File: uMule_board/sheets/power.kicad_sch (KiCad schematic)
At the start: 38 parts, among them Q8 AON6407, U18 TPS62933DRLR, U22 INA219AxD, U28 TLV761

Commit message: all main componenst added. Prepared to change MCU. SCH almost ready
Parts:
- removed D14: SS34, Diode_SMD:D_SMA, symbol PCM_Diode_Schottky_AKL:SS34
- renumbered C42 to C1, C41 to C10, C43 to C11, C45 to C12, C11 to C13, C12 to C14, C13 to C15, C14 to C16, C38 to C2, C39 to C3, C40 to C4, C44 to C5, C46 to C6, C47 to C7, C35 to C8, C37 to C9, D16 to D2, D20 to D3, D17 to D4, D18 to D5, D19 to D6, F4 to F1, F5 to F2, Q8 to Q1, R59 to R1, R62 to R2, R72 to R3, R58 to R4, R63 to R5, R73 to R6, R60 to R7, R61 to R8, R68 to R9, U18 to U1, U28 to U2, U22 to U3

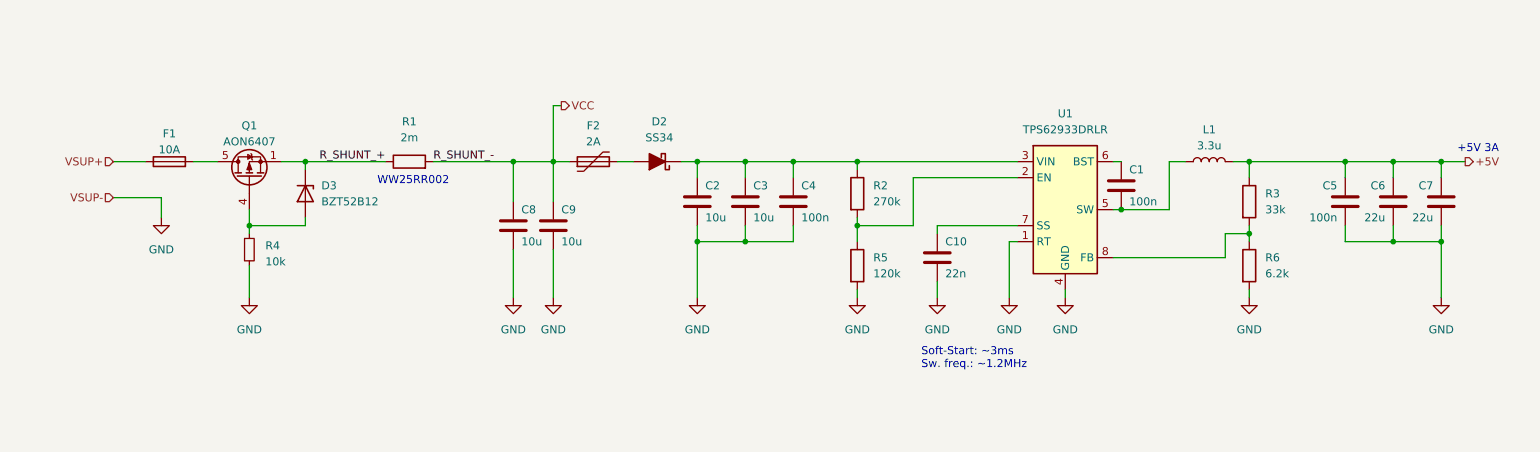
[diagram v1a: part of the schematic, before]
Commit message: Finished schematics. Now ready for PCB
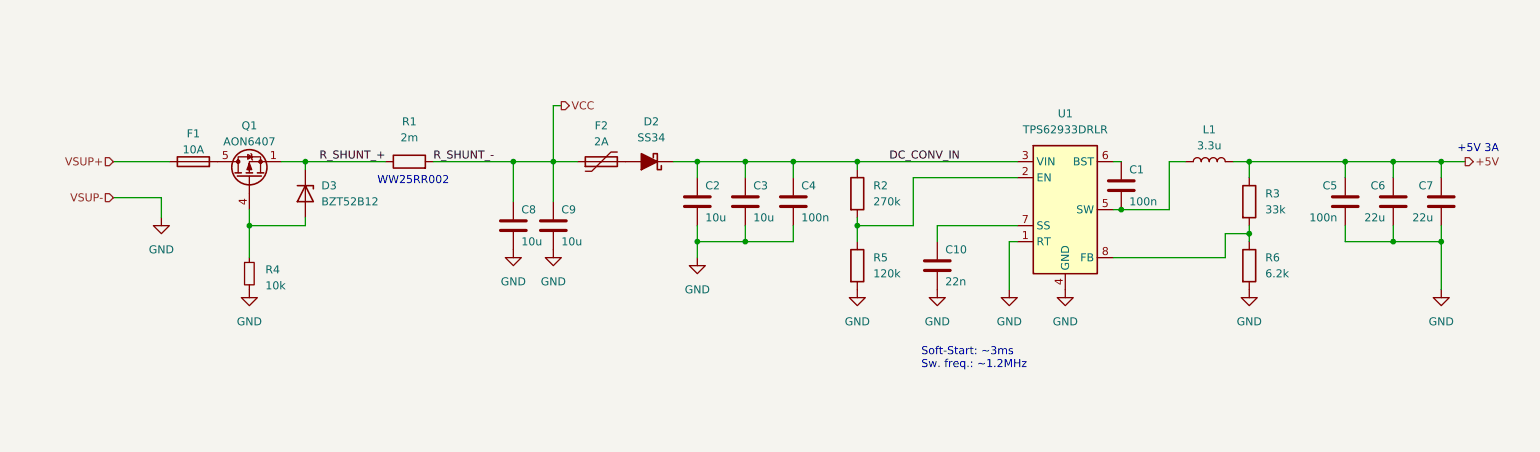
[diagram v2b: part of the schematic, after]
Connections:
- net DC_CONV_IN: now reaches C2.1, C3.1, C4.1, D2.1 (K), R2.1, U1.3 (VIN)
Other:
- moved on the sheet: C10, D2, F1, F2, R4

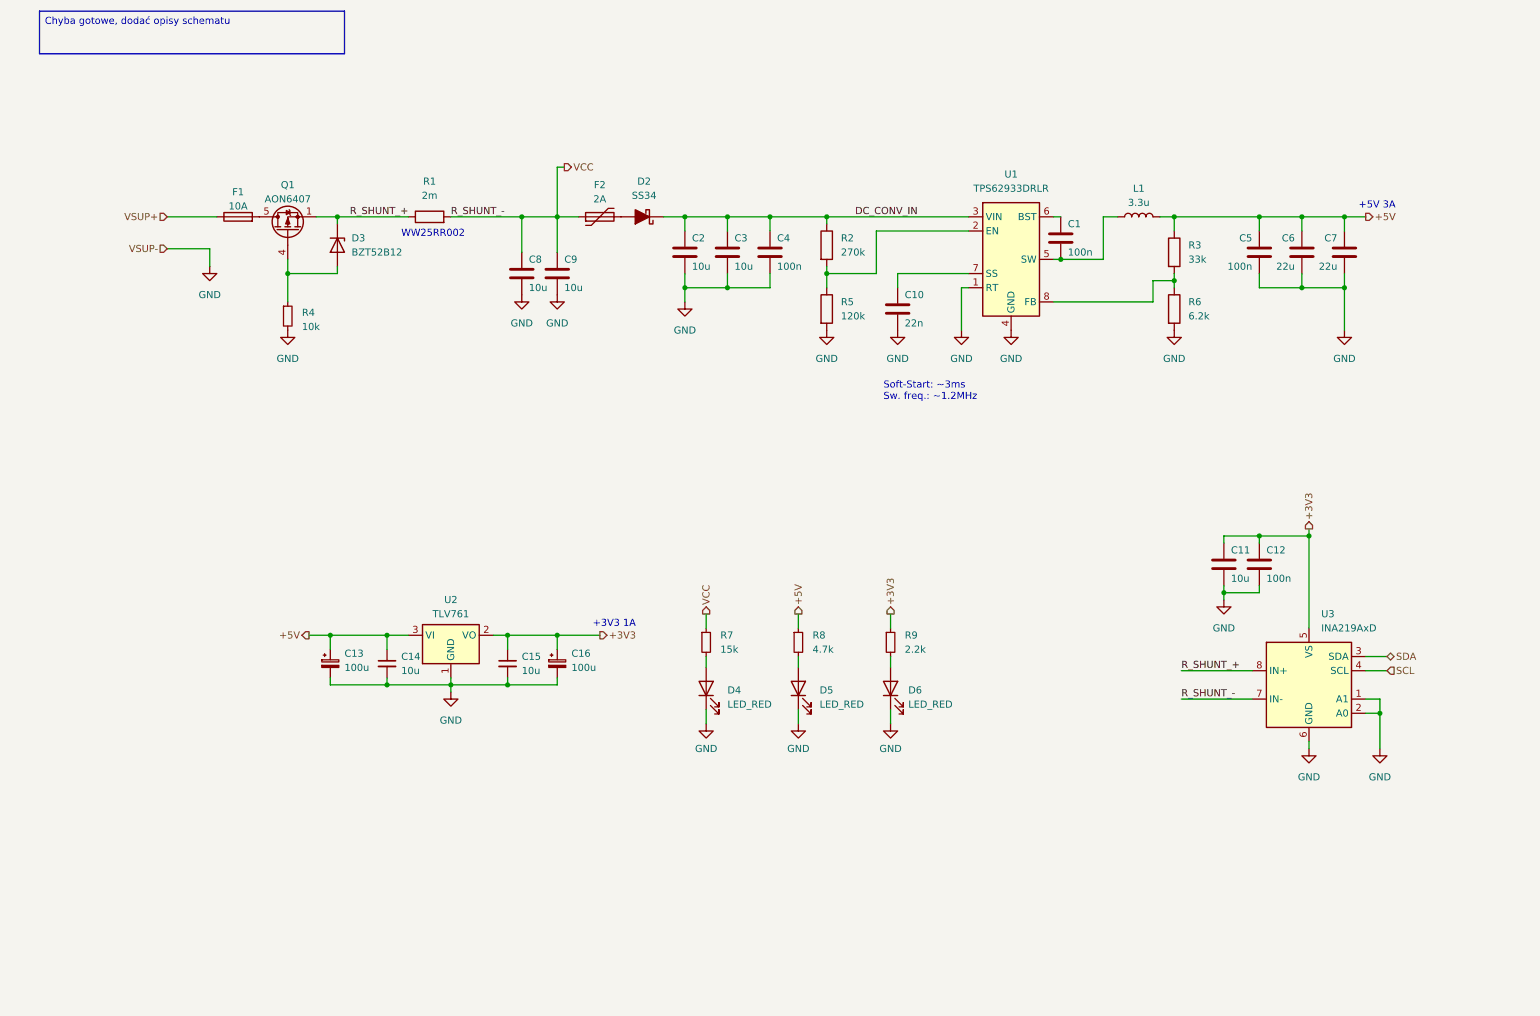
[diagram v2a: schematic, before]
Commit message: Started working on PCB. Ditched high power outputs. Focusing on photodiodes. One commit closer to order
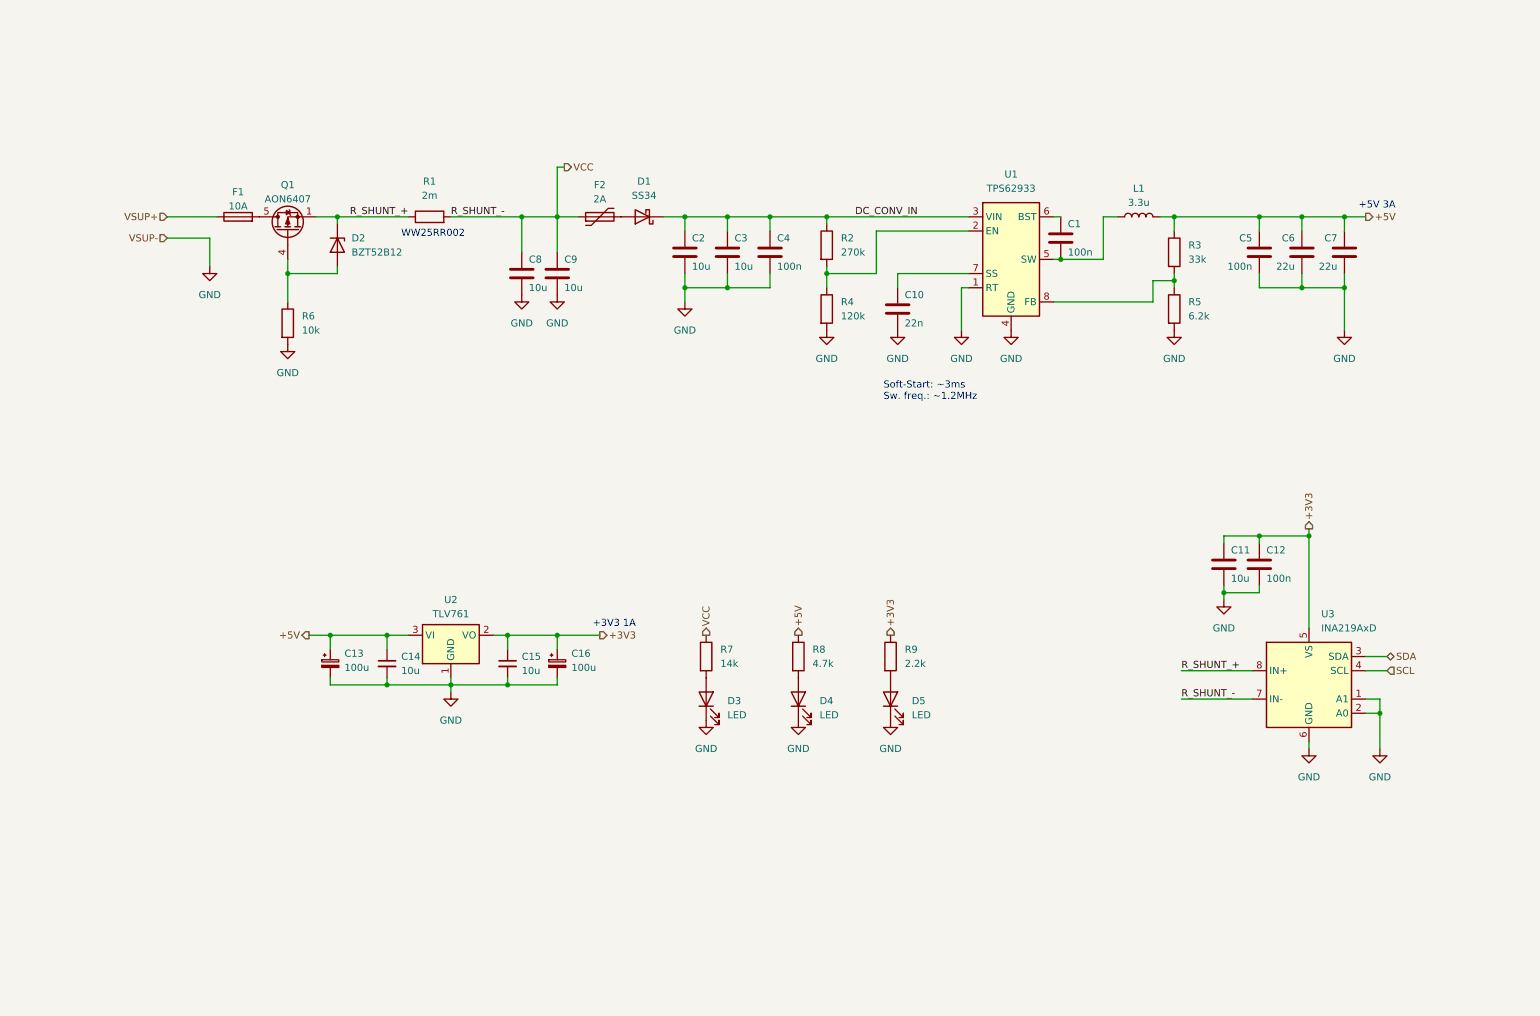
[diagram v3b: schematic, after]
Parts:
- removed D2: SS34, Diode_SMD:D_SMA, symbol PCM_Diode_Schottky_AKL:SS34
- removed D6: LED_RED, LED_SMD:LED_0603_1608Metric, symbol Device:LED
- removed R4: 10k, Resistor_SMD:R_0603_1608Metric, symbol Device:R_Small
- removed R7: 15k, Resistor_SMD:R_0603_1608Metric, symbol Device:R_Small
- removed R8: 4.7k, Resistor_SMD:R_0603_1608Metric, symbol Device:R_Small
- removed R9: 2.2k, Resistor_SMD:R_0603_1608Metric, symbol Device:R_Small
- added D1: SS34, Diode_SMD:D_SMA, symbol Diode:SS34
- added D3: LED, LED_SMD:LED_0603_1608Metric_Pad1.05x0.95mm_HandSolder, symbol Device:LED
- added R6: 10k, Resistor_SMD:R_0603_1608Metric, symbol Device:R
- added R7: 14k, Resistor_SMD:R_0603_1608Metric, symbol Device:R
- added R8: 4.7k, Resistor_SMD:R_0603_1608Metric, symbol Device:R
- added R9: 2.2k, Resistor_SMD:R_0603_1608Metric, symbol Device:R
- D4, D5: value LED_RED -> LED; footprint LED_SMD:LED_0603_1608Metric -> LED_SMD:LED_0603_1608Metric_Pad1.05x0.95mm_HandSolder
- U1: value TPS62933DRLR -> TPS62933
- renumbered D3 to D2, R5 to R4, R6 to R5
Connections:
- net +3V3: now also R9.1
- net +5V: now also R8.1
- net DC_CONV_IN: now also D1.1 (K)
- net GND: now also D3.1 (K), R6.2
- net VCC: now also R7.1
- net at D4.2 (A): now also R8.2
- net at F2.2: now also D1.2 (A)
- net at D5.2 (A): now also R9.2
- net at D2.2 (A), Q1.4 (G): now also R6.1
- new net: D3.2 (A), R7.2
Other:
- title: (none) -> uMule_board

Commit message: removed half phototransistors, etc.
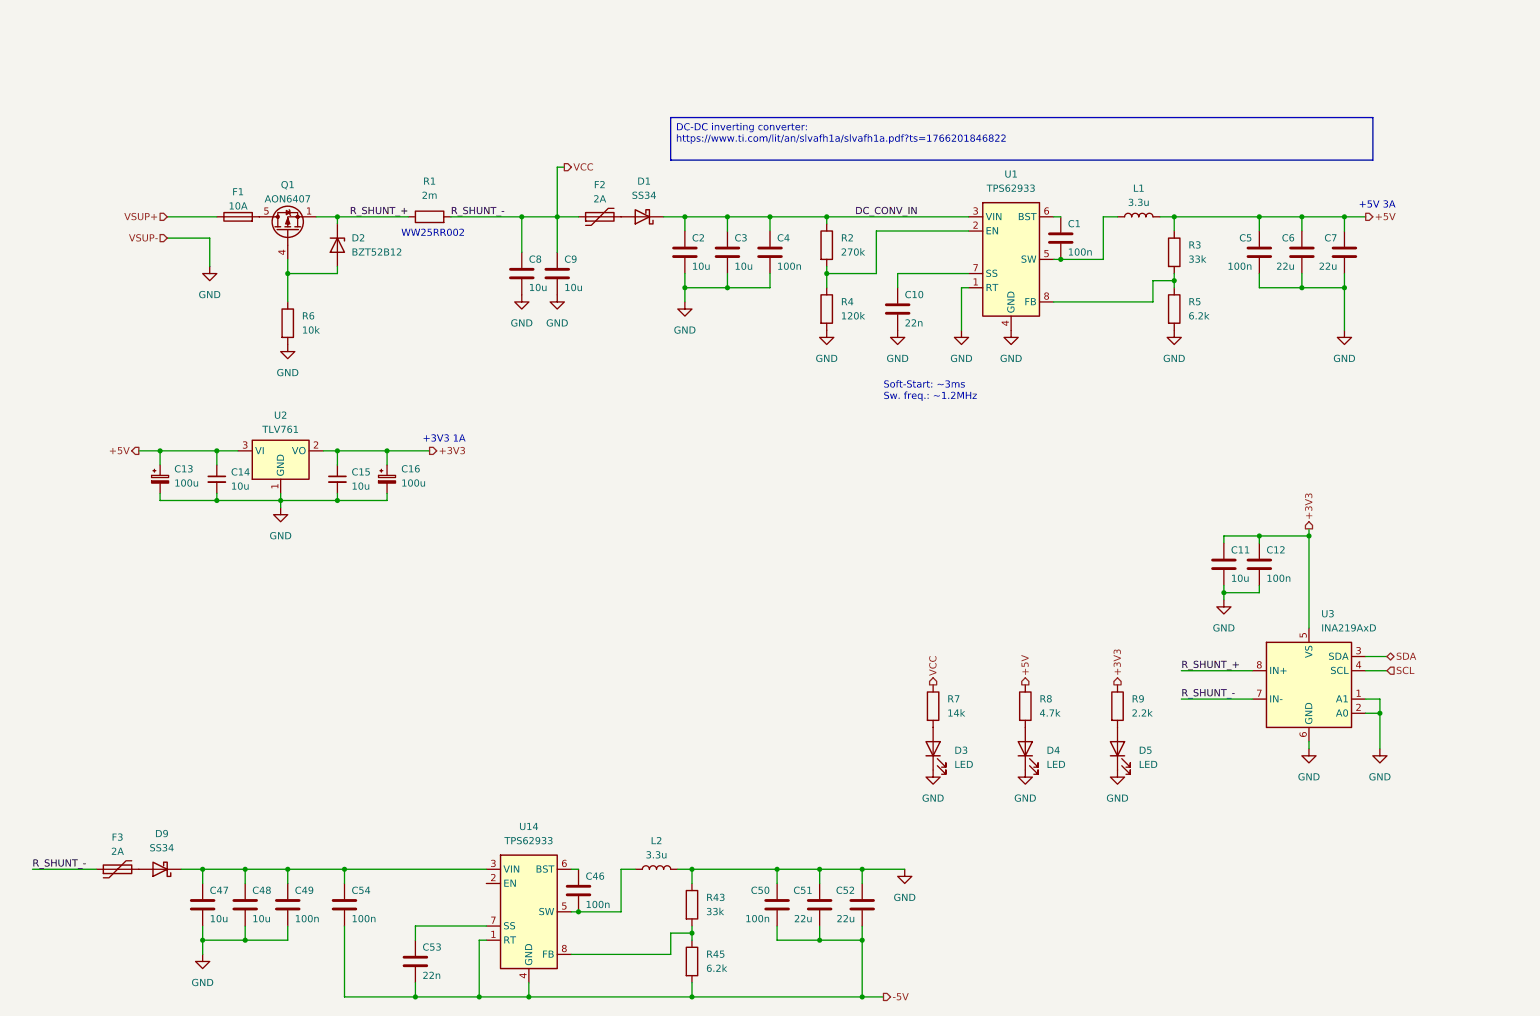
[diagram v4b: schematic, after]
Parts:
- added C46, C49, C50, C54: 100n, Capacitor_SMD:C_0603_1608Metric, symbol Device:C
- added C47, C48: 10u, Capacitor_SMD:C_0805_2012Metric, symbol Device:C
- added C51, C52: 22u, Capacitor_SMD:C_0805_2012Metric, symbol Device:C
- added C53: 22n, Capacitor_SMD:C_0603_1608Metric, symbol Device:C
- added D9: SS34, Diode_SMD:D_SMA, symbol Diode:SS34
- added F3: 2A, Fuse:Fuse_2920_7451Metric, symbol Device:Polyfuse
- added L2: 3.3u, Exit19_kicad_footprints:Inductor_TKD_SPM5030VT, symbol Device:L
- added R43: 33k, Resistor_SMD:R_0603_1608Metric, symbol Device:R
- added R45: 6.2k, Resistor_SMD:R_0603_1608Metric, symbol Device:R
- added U14: TPS62933, Package_TO_SOT_SMD:SOT-583-8, symbol Regulator_Switching:TPS62933
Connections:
- net GND: now also C47.2, C48.2, C49.2, C50.1, C51.1, C52.1, L2.2, R43.1
- net VCC: now also F3.1
- new net: R43.2, R45.1, U14.8 (FB)
- new net: C46.2, L2.1, U14.5 (SW)
- new net: C53.1, U14.7 (SS)
- new net: C47.1, C48.1, C49.1, C54.1, D9.1 (K), U14.3 (VIN)
- new net: D9.2 (A), F3.2
- new net: C46.1, U14.6 (BST)
- new net -5V: C50.2, C51.2, C52.2, C53.2, C54.2, R45.2, U14.1 (RT), U14.4 (GND)
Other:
- moved on the sheet: C13, C14, C15, C16, D3, D4, D5, R7, R8, R9, U2

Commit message: sch ready, only missing the pcb
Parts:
- added C18: 10u, Capacitor_SMD:C_0805_2012Metric, symbol Device:C
- added C26: 22u, Capacitor_SMD:C_0805_2012Metric, symbol Device:C
- added D4: LED, LED_SMD:LED_0603_1608Metric_Pad1.05x0.95mm_HandSolder, symbol Device:LED
- added Q2: S9015, Package_TO_SOT_SMD:SOT-23, symbol My_elemets:S9015
- added R10: 20k, Resistor_SMD:R_0603_1608Metric, symbol Device:R
- added R11: 12k, Resistor_SMD:R_0603_1608Metric, symbol Device:R
- added R12, R8: 10k, Resistor_SMD:R_0603_1608Metric, symbol Device:R
- added R13: 4.7k, Resistor_SMD:R_0603_1608Metric, symbol Device:R
- added R7: 51k, Resistor_SMD:R_0603_1608Metric, symbol Device:R
- added R9: 62k, Resistor_SMD:R_0603_1608Metric, symbol Device:R
- added U3: LM431BMC3, Package_TO_SOT_SMD:SOT-23, symbol My_elemets:LM431BMC3
- R4: value 120k -> 470k
- renumbered C13 to C11, C14 to C12, C15 to C13, C16 to C14, C11 to C15, C12 to C16, C46 to C17, C47 to C19, C48 to C20, C49 to C21, C54 to C22, C50 to C23, C51 to C24, C52 to C25, C53 to C27, D9 to D3, D3 to D5, D4 to D6, D5 to D7, R7 to R14, R8 to R15, R9 to R16, R43 to R17, R45 to R18, U3 to U4, U14 to U5
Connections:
- net -5V: now also C26.2, R11.2, R13.1
- net GND: now also C18.2, C26.1, D4.2 (A), R12.2, U3.3 (A)
- net INV_CONV_IN: now reaches C19.1, C20.1, C21.1, C22.1, D3.1 (K), U5.3 (VIN)
- net INV_CONV_IN: now also C18.1, Q2.3 (C), R10.1, R7.2
- net EN_INV: now reaches U5.2 (EN)
- net EN_INV: now also R11.1, R9.2
- new net: R10.2, R12.1, U3.2 (REF)
- new net: R7.1, R8.1, U3.1 (K)
- new net: Q2.1 (B), R8.2
- new net: Q2.2 (E), R9.1
- new net: D4.1 (K), R13.2
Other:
- moved on the sheet: C1, C10, C11, C12, C13, C14, C15, C16, C17, C19, C2, C20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

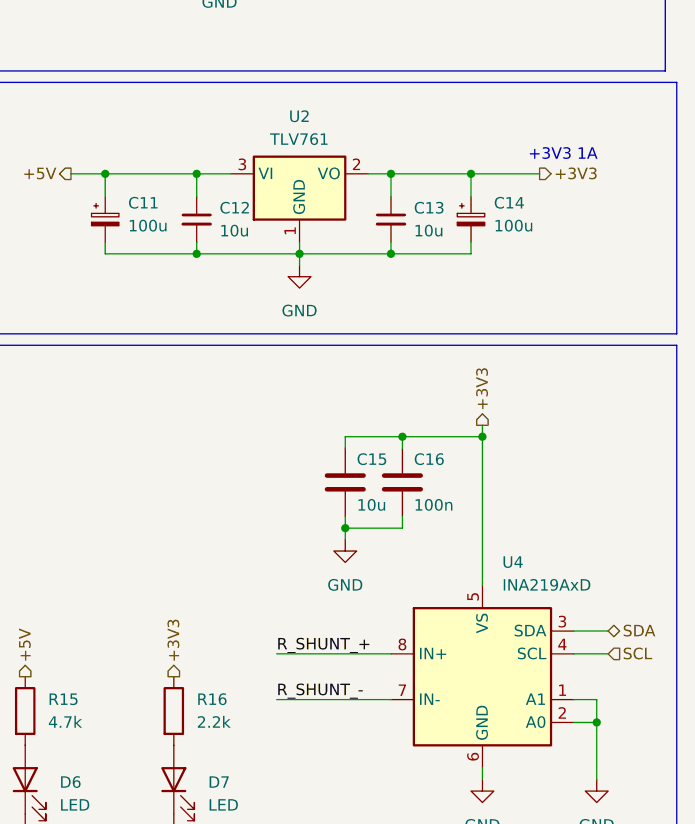
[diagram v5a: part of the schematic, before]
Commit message: DRC Passed, now only slight modifications on traces left, lenght matching and proper board description
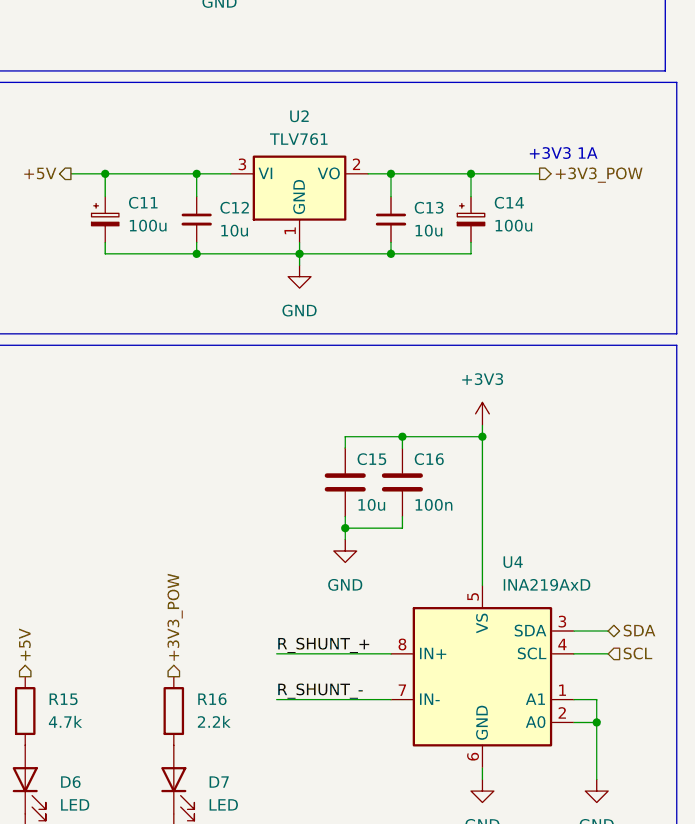
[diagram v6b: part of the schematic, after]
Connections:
- net +3V3: no longer C13.1, C14.1, R16.1, U2.2 (VO)
- new net +3V3_POW: C13.1, C14.1, R16.1, U2.2 (VO)
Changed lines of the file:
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@@
 		)
 	)
-	(hierarchical_label "+3V3"
+	(hierarchical_label "VCC"
 		(shape output)
-		(at 228.6 135.89 90)
+		(at 195.58 135.89 90)
 		(effects
 			(font
@@
 		)
 	)
-	(hierarchical_label "VCC"
+	(hierarchical_label "+3V3_POW"
 		(shape output)
-		(at 195.58 135.89 90)
+		(at 269.24 80.01 0)
 		(effects
 			(font
@@
 		)
 	)
-	(hierarchical_label "+3V3"
-		(shape output)
-		(at 262.89 107.95 90)
-		(effects
-			(font
-				(size 1.27 1.27)
-			)
-			(justify left)
-		)
-	)
-	(hierarchical_label "+3V3"
+	(hierarchical_label "+3V3_POW"
 		(shape output)
-		(at 269.24 80.01 0)
+		(at 228.6 135.89 90)
 		(effects
 			(font
@@
 					(unit 1)
 				)
+			)
+		)
+	)
+	(symbol
+		(lib_id "power:+3V3")
+		(at 262.89 107.95 0)
+		(unit 1)
+		(exclude_from_sim no)
+		(in_bom yes)
+		(on_board yes)
+		(dnp no)
+		(fields_autoplaced yes)
+		(property "Reference" "#PWR095"
+			(at 262.89 111.76 0)
+			(effects
+				(font
+					(size 1.27 1.27)
+				)
+				(hide yes)
+			)
+		)
+		(property "Value" "+3V3"
+			(at 262.89 102.87 0)
+			(effects
+				(font
+					(size 1.27 1.27)
+				)
+			)
+		)
+		(property "Footprint" ""
+			(at 262.89 107.95 0)
+			(effects
+				(font
+					(size 1.27 1.27)
+				)
+				(hide yes)
+			)
+		)
+		(property "Datasheet" ""
+			(at 262.89 107.95 0)
+			(effects
+				(font
+					(size 1.27 1.27)
+				)
+				(hide yes)
+			)
+		)
+		(property "Description" "Power symbol creates a global label with name \"+3V3\""
+			(at 262.89 107.95 0)
+			(effects
+				(font
+					(size 1.27 1.27)
+				)
+				(hide yes)
+			)
+		)
+		(pin "1"
+		)
+		(instances
+			(project ""
+				(path "/3d853824-a92e-40a5-ad1a-5052c8a0bd68/c8adc386-f81e-4a8b-ad62-a18d431f411c"
+					(reference "#PWR095")
+					(unit 1)
+				)
